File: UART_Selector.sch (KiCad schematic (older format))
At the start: 2 parts, among them U201 74HCT125, U202 7400

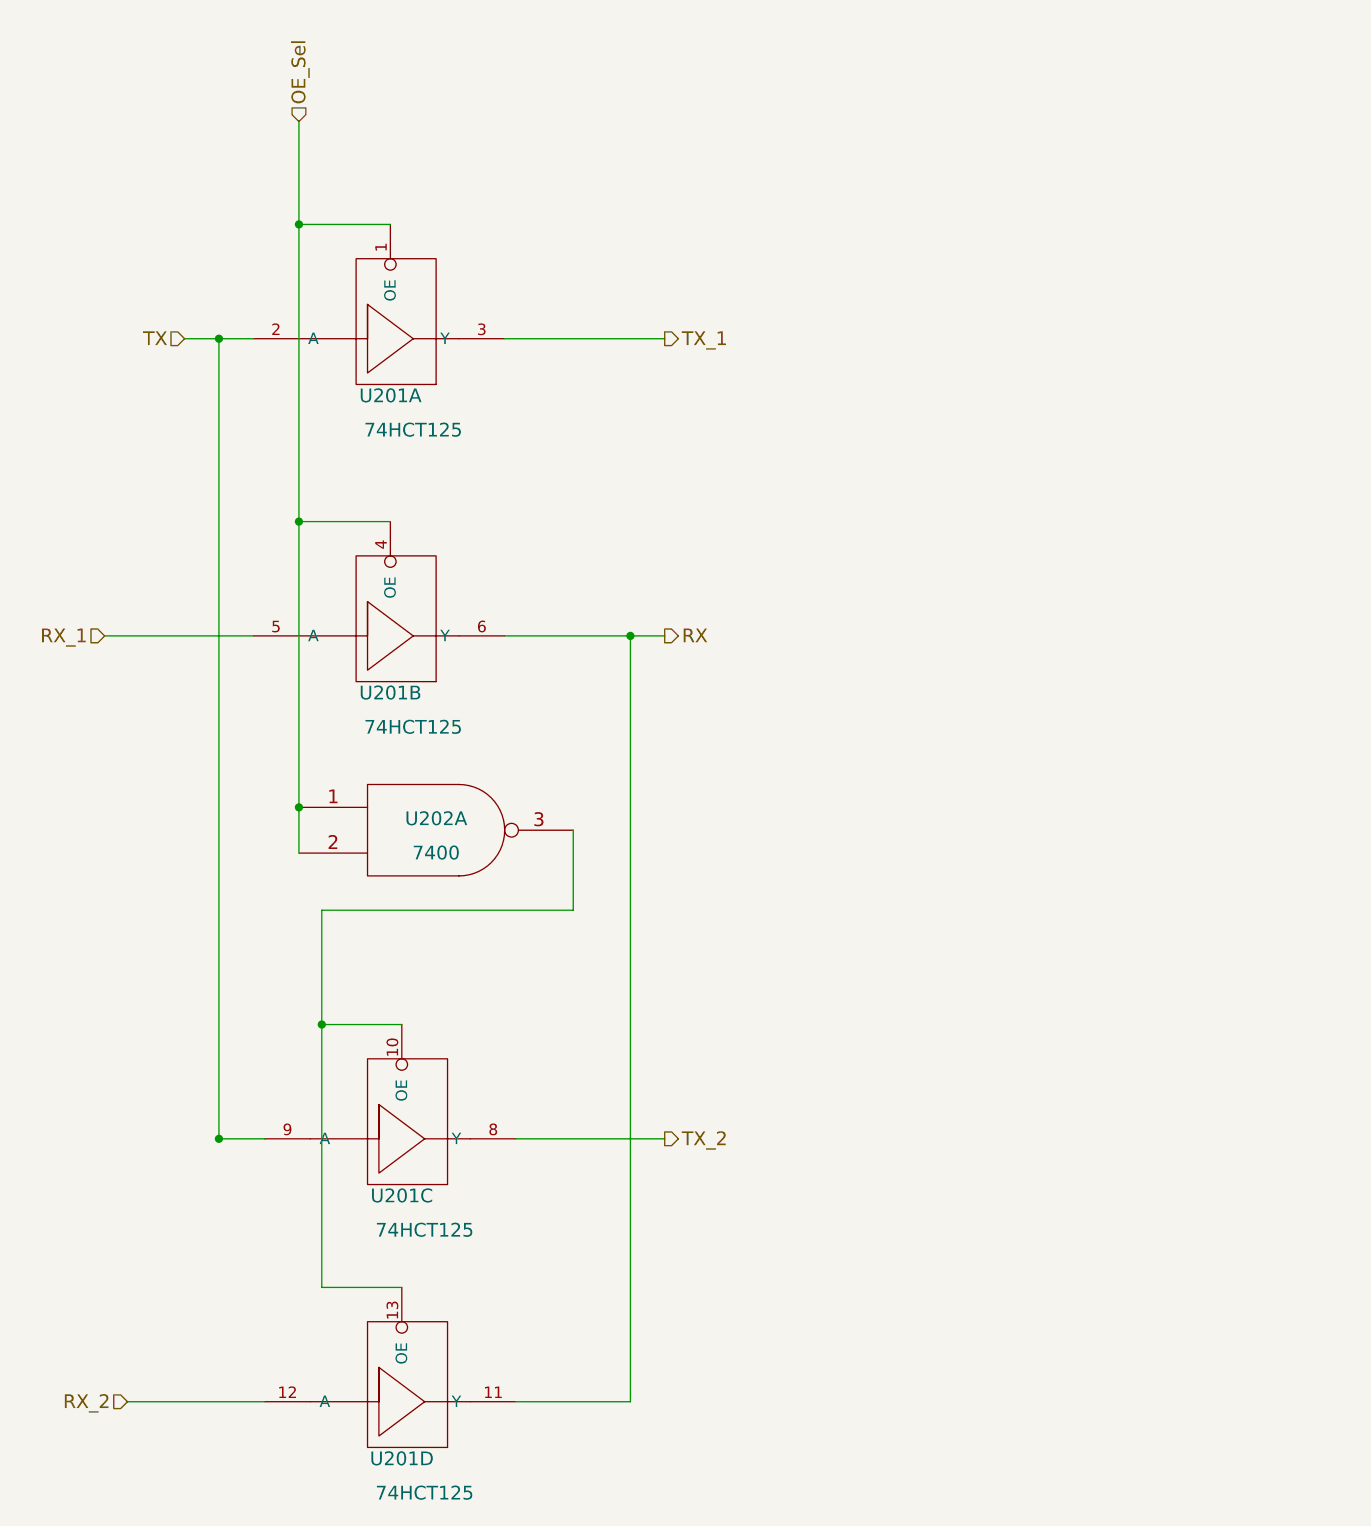
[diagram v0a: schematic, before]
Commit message: Add mechanism to disable UART selector
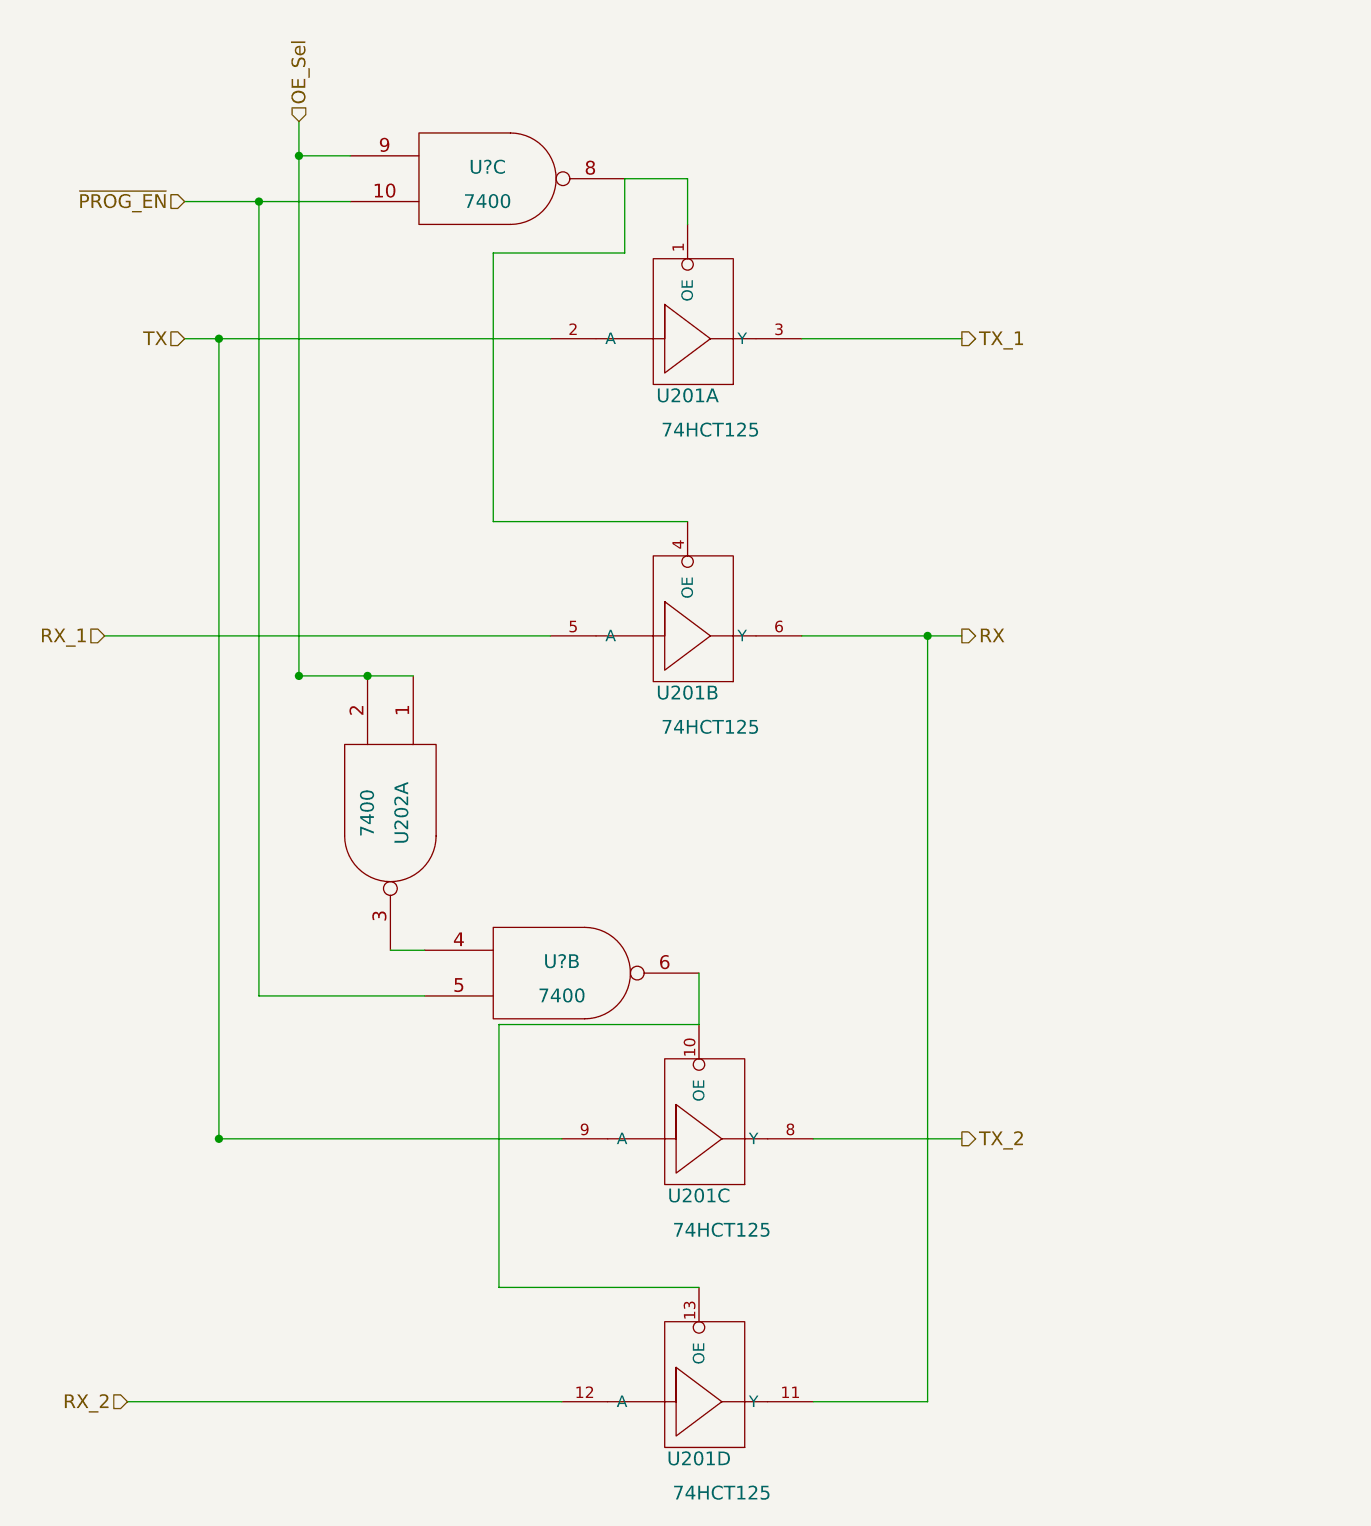
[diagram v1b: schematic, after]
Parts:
- added U? (x2): 7400, symbol 7400
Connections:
- net GND: now also U?.7 (GND), U?.7 (GND)
- net OE_Sel: now also U?.9; no longer U201.1 (OE), U201.4 (OE)
- net VCC: now also U?.14 (VCC), U?.14 (VCC)
- net at U201.10 (OE), U201.13 (OE): now also U?.6; no longer U202.3
- new net: U201.1 (OE), U201.4 (OE), U?.8
- new net: U202.3, U?.4
- new net ~PROG_EN: U?.10, U?.5
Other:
- moved on the sheet: U201A, U201B, U201C, U201D, U202A
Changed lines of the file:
@@
 L 74HCT125 U201
 U 1 1 55335E46
-P 3300 2550
-F 0 "U201" H 3200 2700 60  0000 C CNN
-F 1 "74HCT125" H 3300 2550 60  0000 C CNN
-F 2 "" H 3300 2550 60  0000 C CNN
-F 3 "" H 3300 2550 60  0000 C CNN
-	1    3300 2550
+P 4600 2550
+F 0 "U201" H 4500 2700 60  0000 C CNN
+F 1 "74HCT125" H 4600 2550 60  0000 C CNN
+F 2 "" H 4600 2550 60  0000 C CNN
+F 3 "" H 4600 2550 60  0000 C CNN
+	1    4600 2550
 	1    0    0    -1
 $EndComp
@@
 L 74HCT125 U201
 U 2 1 55335E68
-P 3300 3850
-F 0 "U201" H 3200 4000 60  0000 C CNN
-F 1 "74HCT125" H 3300 3850 60  0000 C CNN
-F 2 "" H 3300 3850 60  0000 C CNN
-F 3 "" H 3300 3850 60  0000 C CNN
-	2    3300 3850
+P 4600 3850
+F 0 "U201" H 4500 4000 60  0000 C CNN
+F 1 "74HCT125" H 4600 3850 60  0000 C CNN
+F 2 "" H 4600 3850 60  0000 C CNN
+F 3 "" H 4600 3850 60  0000 C CNN
+	2    4600 3850
 	1    0    0    -1
 $EndComp
@@
 L 74HCT125 U201
 U 3 1 55335E96
-P 3350 6050
-F 0 "U201" H 3250 6200 60  0000 C CNN
-F 1 "74HCT125" H 3350 6050 60  0000 C CNN
-F 2 "" H 3350 6050 60  0000 C CNN
-F 3 "" H 3350 6050 60  0000 C CNN
-	3    3350 6050
+P 4650 6050
+F 0 "U201" H 4550 6200 60  0000 C CNN
+F 1 "74HCT125" H 4650 6050 60  0000 C CNN
+F 2 "" H 4650 6050 60  0000 C CNN
+F 3 "" H 4650 6050 60  0000 C CNN
+	3    4650 6050
 	1    0    0    -1
 $EndComp
@@
 L 7400 U202
 U 1 1 55335F93
-P 3400 4300
-F 0 "U202" H 3400 4350 60  0000 C CNN
-F 1 "7400" H 3400 4200 60  0000 C CNN
-F 2 "" H 3400 4300 60  0000 C CNN
-F 3 "" H 3400 4300 60  0000 C CNN
-	1    3400 4300
-	1    0    0    -1
+P 3200 4225
+F 0 "U202" H 3200 4275 60  0000 C CNN
+F 1 "7400" H 3200 4125 60  0000 C CNN
+F 2 "" H 3200 4225 60  0000 C CNN
+F 3 "" H 3200 4225 60  0000 C CNN
+	1    3200 4225
+	0    1    1    0
 $EndComp
-Text HLabel 4400 2150 2    60   Output ~ 0
+Text HLabel 5700 2150 2    60   Output ~ 0
 TX_1
-Text HLabel 4400 5650 2    60   Output ~ 0
+Text HLabel 5700 5650 2    60   Output ~ 0
 TX_2
 Wire Wire Line
-	3700 2150 4400 2150
+	5000 2150 5700 2150
 Wire Wire Line
-	3200 2950 2800 2950
-Wire Wire Line
-	2800 1200 2800 4400
-Connection ~ 2800 1650
-Connection ~ 2800 2950
-Connection ~ 2800 4200
-Wire Wire Line
-	3250 6300 2900 6300
-Wire Wire Line
-	2900 6300 2900 4650
-Wire Wire Line
-	2900 4650 4000 4650
-Wire Wire Line
-	4000 4650 4000 4300
-Wire Wire Line
-	3250 5150 2900 5150
-Connection ~ 2900 5150
-Wire Wire Line
-	3750 5650 4400 5650
+	5050 5650 5700 5650
 Text HLabel 2050 6800 0    60   Input ~ 0
 RX_2
-Text HLabel 4400 3450 2    60   Output ~ 0
+Text HLabel 5700 3450 2    60   Output ~ 0
 RX
 Text HLabel 2800 1200 1    60   Input ~ 0
 OE_Sel
 Wire Wire Line
-	3700 3450 4400 3450
-Connection ~ 4250 3450
+	5000 3450 5700 3450
+Connection ~ 5550 3450
 $Comp
 L 74HCT125 U201
 U 4 1 553360DE
-P 3350 7200
-F 0 "U201" H 3250 7350 60  0000 C CNN
-F 1 "74HCT125" H 3350 7200 60  0000 C CNN
-F 2 "" H 3350 7200 60  0000 C CNN
-F 3 "" H 3350 7200 60  0000 C CNN
-	4    3350 7200
+P 4650 7200
+F 0 "U201" H 4550 7350 60  0000 C CNN
+F 1 "74HCT125" H 4650 7200 60  0000 C CNN
+F 2 "" H 4650 7200 60  0000 C CNN
+F 3 "" H 4650 7200 60  0000 C CNN
+	4    4650 7200
 	1    0    0    -1
 $EndComp
 Wire Wire Line
-	4250 6800 3750 6800
+	5550 6800 5050 6800
 Wire Wire Line
-	4250 3450 4250 6800
+	5550 3450 5550 6800
 Wire Wire Line
-	2600 3450 1950 3450
+	1950 3450 3900 3450
 Text HLabel 2300 2150 0    60   Input ~ 0
 TX
 Wire Wire Line
-	3200 1650 2800 1650
-Wire Wire Line
-	2300 2150 2600 2150
+	2300 2150 3900 2150
 Wire Wire Line
 	2450 2150 2450 5650
@@
 Connection ~ 2450 2150
 Wire Wire Line
-	2450 5650 2650 5650
+	2450 5650 3950 5650
 Wire Wire Line
-	2650 6800 2050 6800
+	2050 6800 3950 6800
+Text HLabel 2300 1550 0    60   Input ~ 0
+~PROG_EN
+$Comp
+L 7400 U?
+U 3 1 5590F692
+P 3625 1450
+F 0 "U?" H 3625 1500 60  0000 C CNN
+F 1 "7400" H 3625 1350 60  0000 C CNN
+F 2 "" H 3625 1450 60  0000 C CNN
+F 3 "" H 3625 1450 60  0000 C CNN
+	3    3625 1450
+	1    0    0    -1
+$EndComp
+$Comp
+L 7400 U?
+U 2 1 5590FA08
+P 3950 4925
+F 0 "U?" H 3950 4975 60  0000 C CNN
+F 1 "7400" H 3950 4825 60  0000 C CNN
+F 2 "" H 3950 4925 60  0000 C CNN
+F 3 "" H 3950 4925 60  0000 C CNN
+	2    3950 4925
+	1    0    0    -1
+$EndComp
+Wire Wire Line
+	2800 3625 3300 3625
+Connection ~ 2800 3625
+Connection ~ 3100 3625
+Wire Wire Line
+	3200 4825 3350 4825
+Wire Wire Line
+	4550 4925 4550 5150
+Wire Wire Line
+	4500 1450 4500 1650
+Wire Wire Line
+	2800 1200 2800 3625
+Wire Wire Line
+	2800 1350 3025 1350
+Wire Wire Line
+	2300 1550 3025 1550
+Wire Wire Line
+	4225 1450 4500 1450
+Wire Wire Line
+	4500 2950 3650 2950
+Wire Wire Line
+	3650 2950 3650 1775
+Wire Wire Line
+	3650 1775 4225 1775
+Wire Wire Line
+	4225 1775 4225 1450
+Connection ~ 2800 1350
+Wire Wire Line
+	3350 5025 2625 5025
+Wire Wire Line
+	2625 5025 2625 1550
+Connection ~ 2625 1550
+Wire Wire Line
+	4550 5150 3675 5150
+Wire Wire Line
+	3675 5150 3675 6300
+Wire Wire Line
+	3675 6300 4550 6300
 $EndSCHEMATC

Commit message: Fix pin for ESP
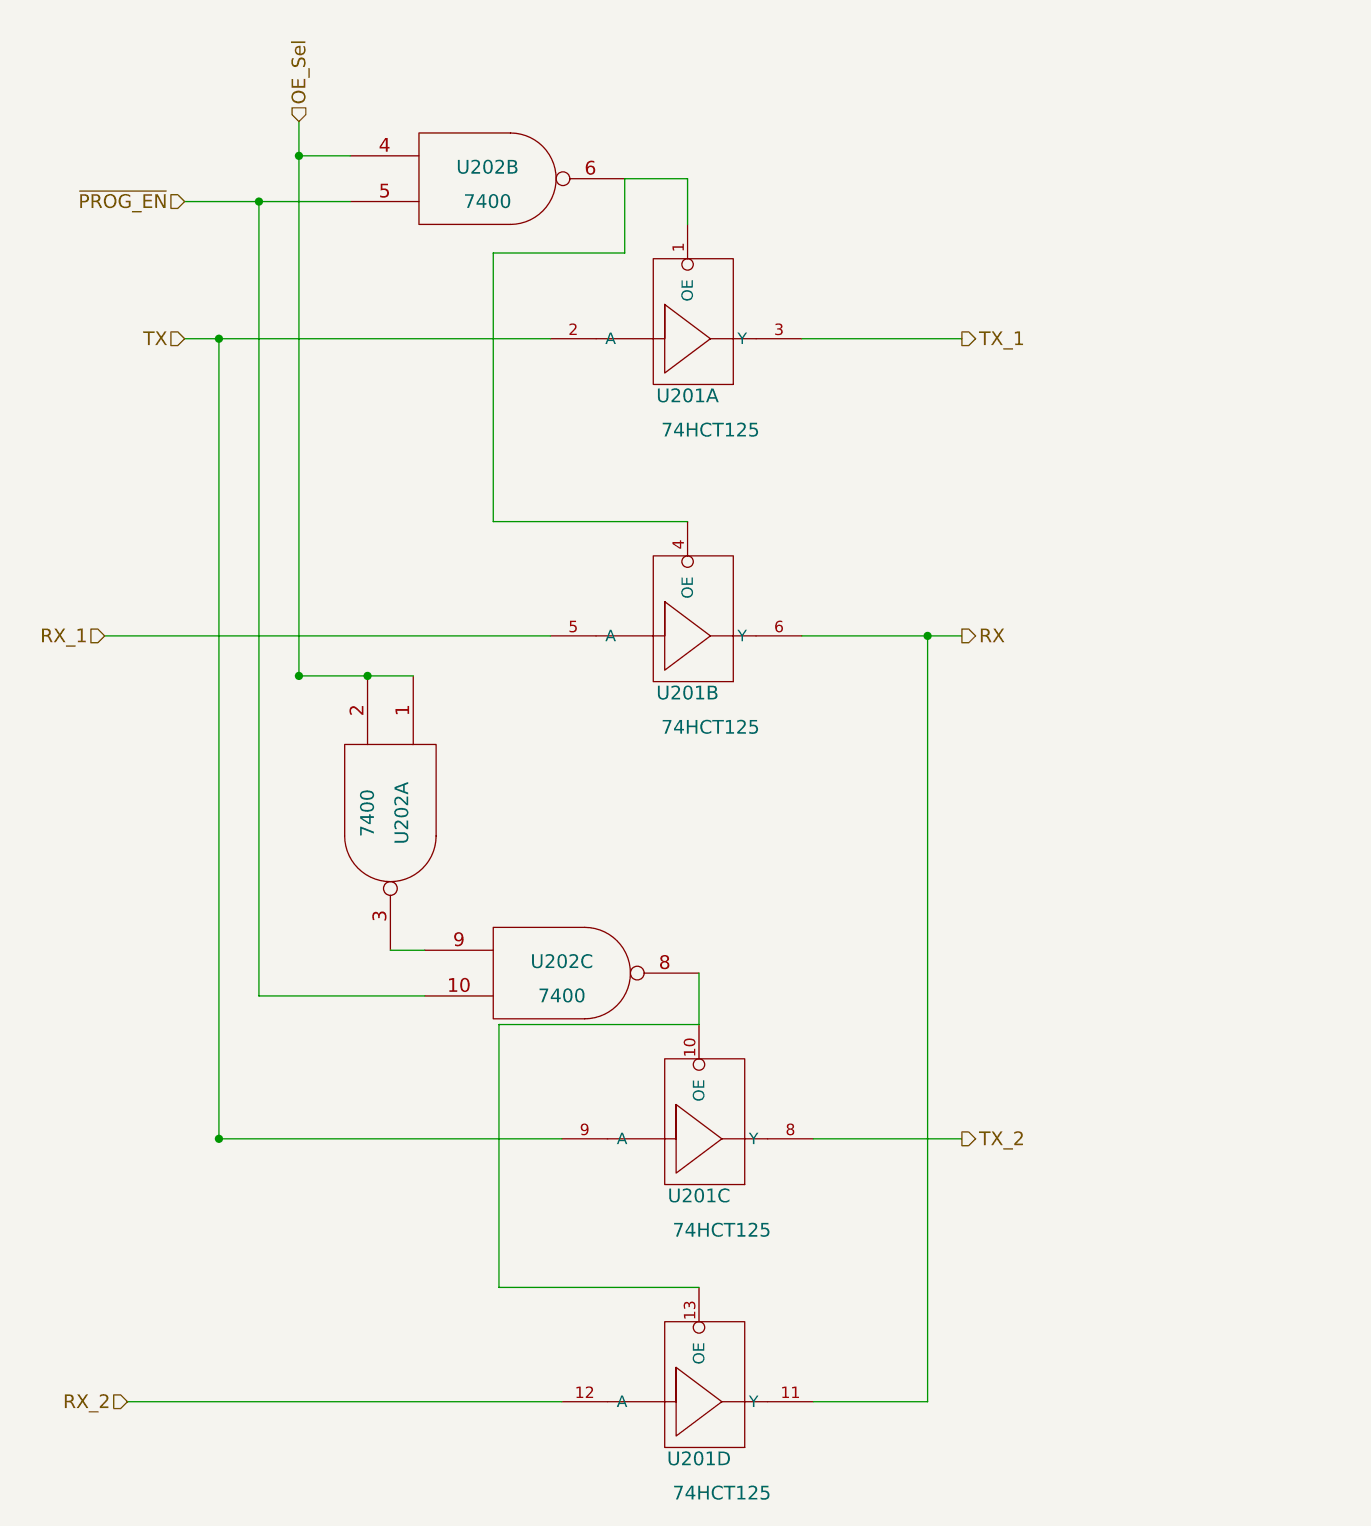
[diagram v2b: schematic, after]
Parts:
- gave numbers to parts that had none: 1
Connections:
- net OE_Sel: now also U202.4; no longer U202.9
- net ~PROG_EN: now also U202.10, U202.5; no longer U202.10, U202.5
- net at U201.1 (OE), U201.4 (OE): now also U202.6; no longer U202.8
- net at U201.10 (OE), U201.13 (OE): now also U202.8; no longer U202.6
- net at U202.3: now also U202.9; no longer U202.4
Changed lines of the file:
@@
 ~PROG_EN
 $Comp
-L 7400 U?
-U 3 1 5590F692
+L 7400 U202
+U 2 1 5590F692
 P 3625 1450
-F 0 "U?" H 3625 1500 60  0000 C CNN
+F 0 "U202" H 3625 1500 60  0000 C CNN
 F 1 "7400" H 3625 1350 60  0000 C CNN
 F 2 "" H 3625 1450 60  0000 C CNN
 F 3 "" H 3625 1450 60  0000 C CNN
-	3    3625 1450
+	2    3625 1450
 	1    0    0    -1
 $EndComp
 $Comp
-L 7400 U?
-U 2 1 5590FA08
+L 7400 U202
+U 3 1 5590FA08
 P 3950 4925
-F 0 "U?" H 3950 4975 60  0000 C CNN
+F 0 "U202" H 3950 4975 60  0000 C CNN
 F 1 "7400" H 3950 4825 60  0000 C CNN
 F 2 "" H 3950 4925 60  0000 C CNN
 F 3 "" H 3950 4925 60  0000 C CNN
-	2    3950 4925
+	3    3950 4925
 	1    0    0    -1
 $EndComp

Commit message: Version 0.2
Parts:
- U201, U202: footprint (none) -> SMD_Packages:SOIC-14_N
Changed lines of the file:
@@
 EESchema Schematic File Version 2
+LIBS:espduino-rescue
 LIBS:power
 LIBS:device
@@
 LIBS:memory
 LIBS:xilinx
-LIBS:special
 LIBS:microcontrollers
 LIBS:dsp
@@
 LIBS:valves
 LIBS:littlebush
+LIBS:ab2_7segment
+LIBS:ab2_audio
+LIBS:ab2_buffer
+LIBS:ab2_capacitor
+LIBS:ab2_connectivity
+LIBS:ab2_dac
+LIBS:ab2_diode
+LIBS:ab2_gpio_expansion
+LIBS:ab2_header
+LIBS:ab2_idc
+LIBS:ab2_inductor
+LIBS:ab2_input_devices
+LIBS:ab2_jumper
+LIBS:ab2_lcd
+LIBS:ab2_led
+LIBS:ab2_opamp
+LIBS:ab2_pot
+LIBS:ab2_power
+LIBS:ab2_regulator
+LIBS:ab2_relay
+LIBS:ab2_resistor
+LIBS:ab2_sensor
+LIBS:ab2_stepper
+LIBS:ab2_supply
+LIBS:ab2_terminal_block
+LIBS:ab2_test
+LIBS:ab2_transistor
+LIBS:ab2_uC
+LIBS:ab2_usb
+LIBS:ab2_xtal
 LIBS:espduino-cache
 EELAYER 25 0
@@
 $Descr A4 11693 8268
 encoding utf-8
-Sheet 2 5
+Sheet 2 6
 Title ""
 Date ""
@@
 F 0 "U201" H 4500 2700 60  0000 C CNN
 F 1 "74HCT125" H 4600 2550 60  0000 C CNN
-F 2 "" H 4600 2550 60  0000 C CNN
+F 2 "SMD_Packages:SOIC-14_N" H 4600 2550 60  0001 C CNN
 F 3 "" H 4600 2550 60  0000 C CNN
 	1    4600 2550
@@
 F 0 "U201" H 4500 4000 60  0000 C CNN
 F 1 "74HCT125" H 4600 3850 60  0000 C CNN
-F 2 "" H 4600 3850 60  0000 C CNN
+F 2 "SMD_Packages:SOIC-14_N" H 4600 3850 60  0001 C CNN
 F 3 "" H 4600 3850 60  0000 C CNN
 	2    4600 3850
@@
 F 0 "U201" H 4550 6200 60  0000 C CNN
 F 1 "74HCT125" H 4650 6050 60  0000 C CNN
-F 2 "" H 4650 6050 60  0000 C CNN
+F 2 "SMD_Packages:SOIC-14_N" H 4650 6050 60  0001 C CNN
 F 3 "" H 4650 6050 60  0000 C CNN
 	3    4650 6050
@@
 F 0 "U202" H 3200 4275 60  0000 C CNN
 F 1 "7400" H 3200 4125 60  0000 C CNN
-F 2 "" H 3200 4225 60  0000 C CNN
+F 2 "SMD_Packages:SOIC-14_N" H 3200 4225 60  0001 C CNN
 F 3 "" H 3200 4225 60  0000 C CNN
 	1    3200 4225
@@
 F 0 "U201" H 4550 7350 60  0000 C CNN
 F 1 "74HCT125" H 4650 7200 60  0000 C CNN
-F 2 "" H 4650 7200 60  0000 C CNN
+F 2 "SMD_Packages:SOIC-14_N" H 4650 7200 60  0001 C CNN
 F 3 "" H 4650 7200 60  0000 C CNN
 	4    4650 7200
@@
 F 0 "U202" H 3625 1500 60  0000 C CNN
 F 1 "7400" H 3625 1350 60  0000 C CNN
-F 2 "" H 3625 1450 60  0000 C CNN
+F 2 "SMD_Packages:SOIC-14_N" H 3625 1450 60  0001 C CNN
 F 3 "" H 3625 1450 60  0000 C CNN
 	2    3625 1450
@@
 F 0 "U202" H 3950 4975 60  0000 C CNN
 F 1 "7400" H 3950 4825 60  0000 C CNN
-F 2 "" H 3950 4925 60  0000 C CNN
+F 2 "SMD_Packages:SOIC-14_N" H 3950 4925 60  0001 C CNN
 F 3 "" H 3950 4925 60  0000 C CNN
 	3    3950 4925

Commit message: Minor changes
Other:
- note added: "74HCT125 missing ground and VCC connectinons"
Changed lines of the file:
@@
 Wire Wire Line
 	3675 6300 4550 6300
+Text Notes 4800 1850 0    60   ~ 0
+74HCT125 missing ground and VCC connectinons
 $EndSCHEMATC
